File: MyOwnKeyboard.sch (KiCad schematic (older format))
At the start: 465 parts, among them J1 Mini-DIN-6, Q1 RFD14N05L, SW1 SW_SPST, SW10 SW_SPST, SW100 SW_SPST, SW101 SW_SPST, SW102 SW_SPST, SW103 SW_SPST, SW104 SW_SPST, SW105 SW_SPST, SW106 SW_SPST, SW107 SW_SPST, SW108 SW_SPST, SW109 SW_SPST, SW11 SW_SPST, SW110 SW_SPST, SW111 SW_SPST, SW112 SW_SPST, SW113 SW_SPST, SW114 SW_SPST, SW12 SW_SPST, SW13 SW_SPST, SW14 SW_SPST, SW15 SW_SPST, SW16 SW_SPST, SW17 SW_SPST, SW18 SW_SPST, SW19 SW_SPST, SW2 SW_SPST, SW20 SW_SPST, SW21 SW_SPST, SW22 SW_SPST, SW23 SW_SPST, SW24 SW_SPST, SW25 SW_SPST, SW26 SW_SPST, SW27 SW_SPST, SW28 SW_SPST, SW29 SW_SPST, SW3 SW_SPST, SW30 SW_SPST, SW31 SW_SPST, SW32 SW_SPST, SW33 SW_SPST, SW34 SW_SPST, SW35 SW_SPST, SW36 SW_SPST, SW37 SW_SPST, SW38 SW_SPST, SW39 SW_SPST, SW4 SW_SPST, SW40 SW_SPST, SW41 SW_SPST, SW42 SW_SPST, SW43 SW_SPST, SW44 SW_SPST, SW45 SW_SPST, SW46 SW_SPST, SW47 SW_SPST, SW48 SW_SPST, SW49 SW_SPST, SW5 SW_SPST, SW50 SW_SPST, SW51 SW_SPST, SW52 SW_SPST, SW53 SW_SPST, SW54 SW_SPST, SW55 SW_SPST, SW56 SW_SPST, SW57 SW_SPST, SW58 SW_SPST, SW59 SW_SPST, SW6 SW_SPST, SW60 SW_SPST, SW61 SW_SPST, SW62 SW_SPST, SW63 SW_SPST, SW64 SW_SPST, SW65 SW_SPST, SW66 SW_SPST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

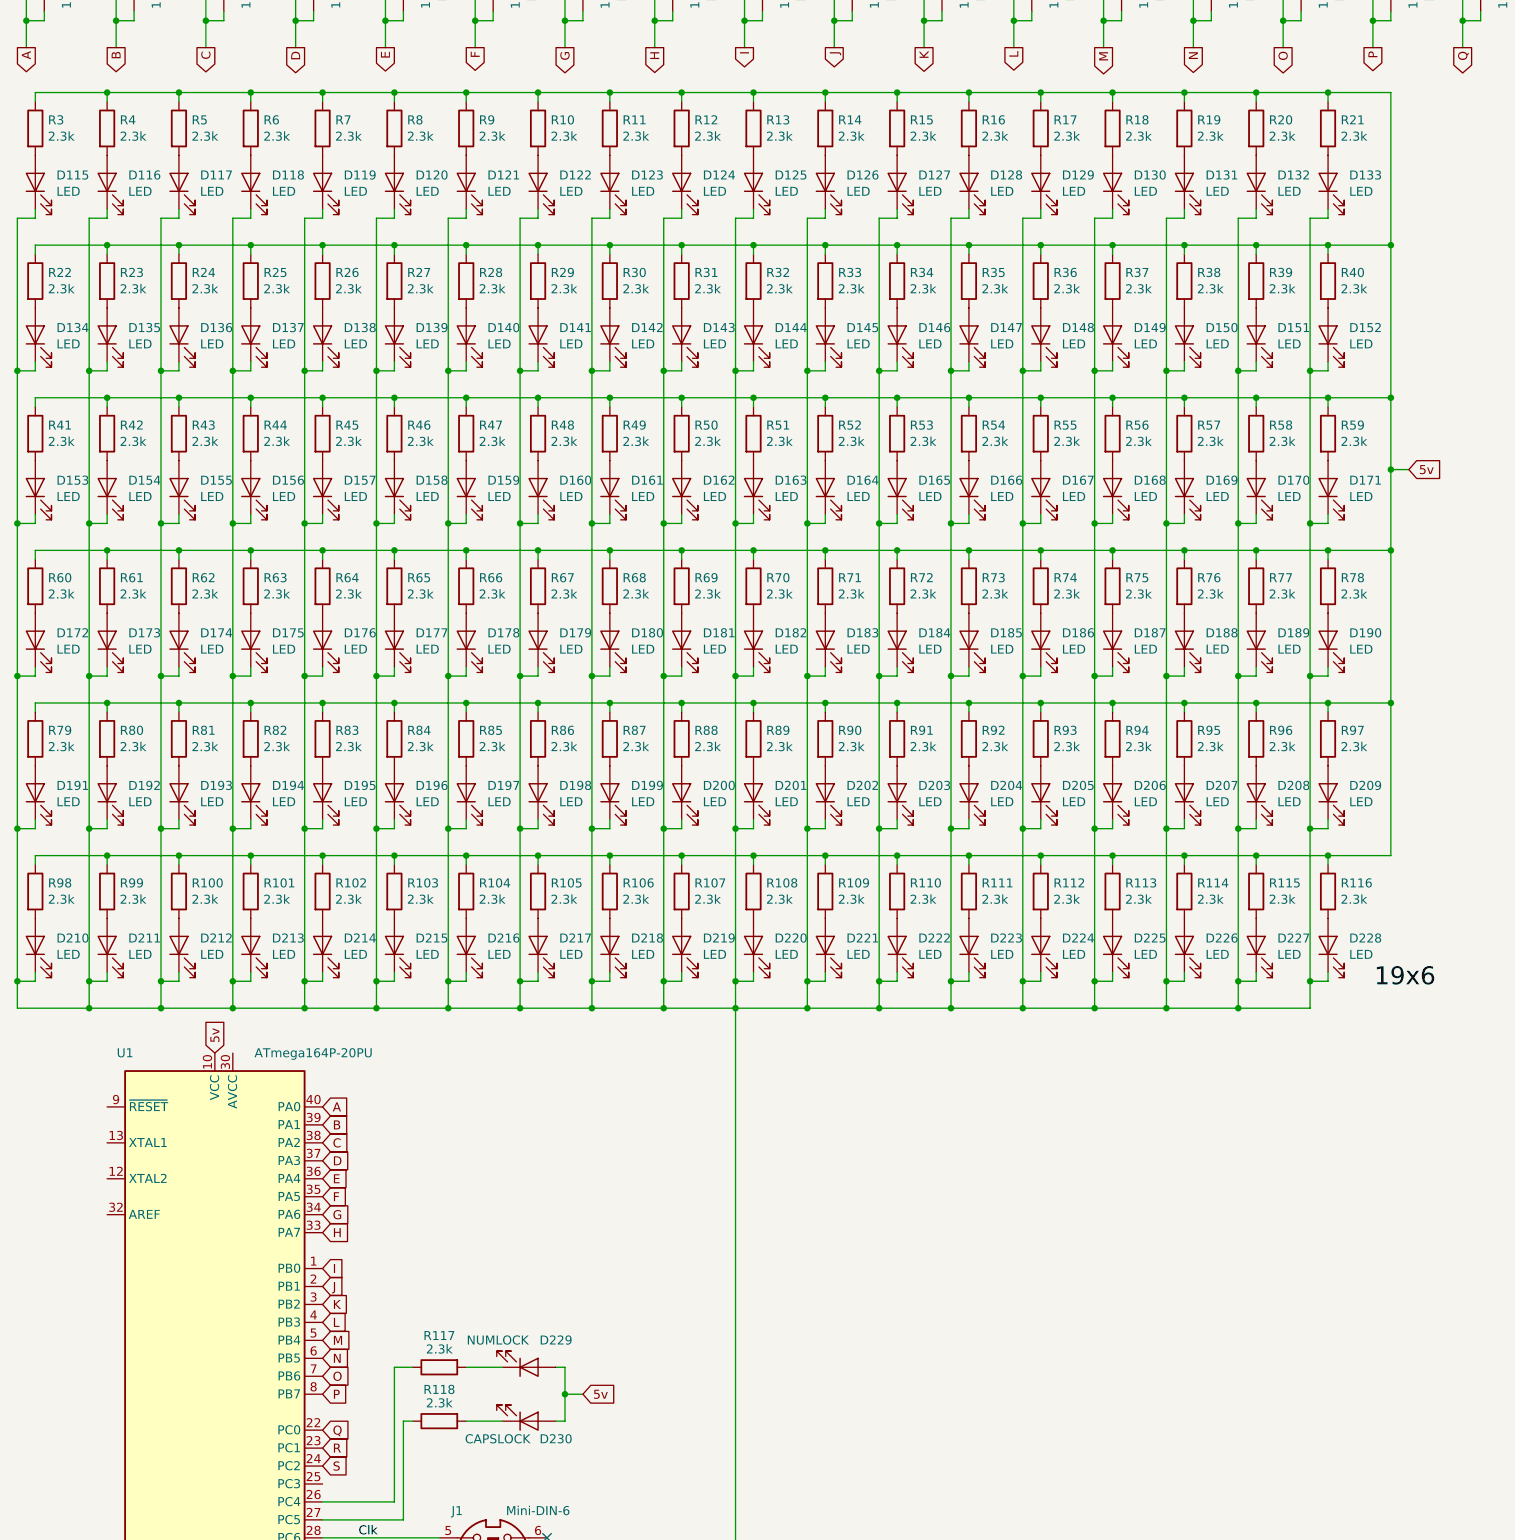
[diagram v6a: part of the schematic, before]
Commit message: Update resistor values to squeeze out some of that sweet, sweet current
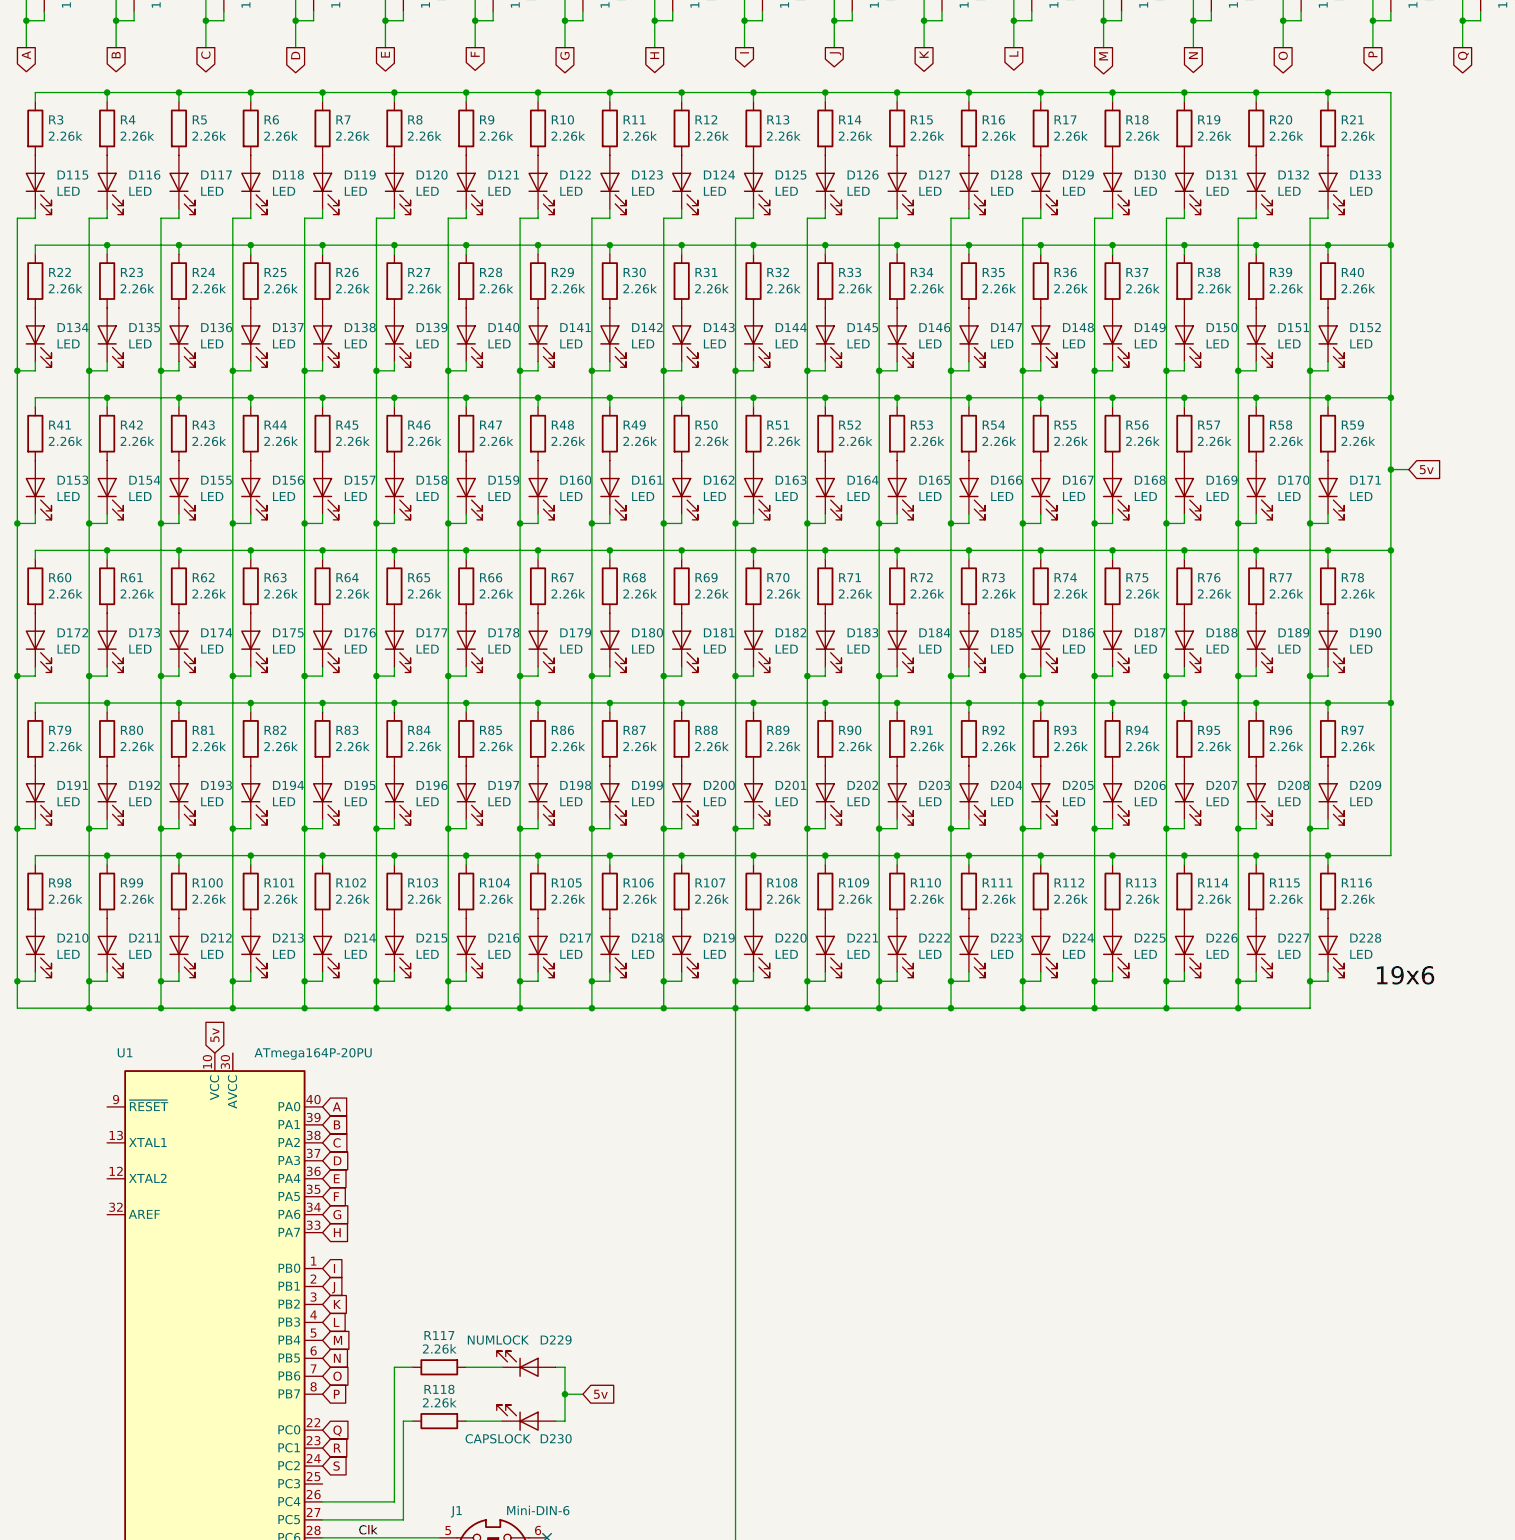
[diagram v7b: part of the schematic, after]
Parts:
- R10, R100, R101, R102, R103, R104, R105, R106, R107, R108, R109, R11, R110, R111, R112, R113, R114, R115, R116, R117, R118, R12, R13, R14, R15, R16, R17, R18, R19, R20, R21, R22, R23, R24, R25, R26, R27, R28, R29, R3, R30, R31, R32, R33, R34, R35, R36, R37, R38, R39, R4, R40, R41, R42, R43, R44, R45, R46, R47, R48, R49, R5, R50, R51, R52, R53, R54, R55, R56, R57, R58, R59, R6, R60, R61, R62, R63, R64, R65, R66, R67, R68, R69, R7, R70, R71, R72, R73, R74, R75, R76, R77, R78, R79, R8, R80, R81, R82, R83, R84, R85, R86, R87, R88, R89, R9, R90, R91, R92, R93, R94, R95, R96, R97, R98, R99: value 2.3k -> 2.26k
